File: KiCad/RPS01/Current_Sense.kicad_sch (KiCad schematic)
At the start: 4 parts, among them U8 INA139QPWRQ1

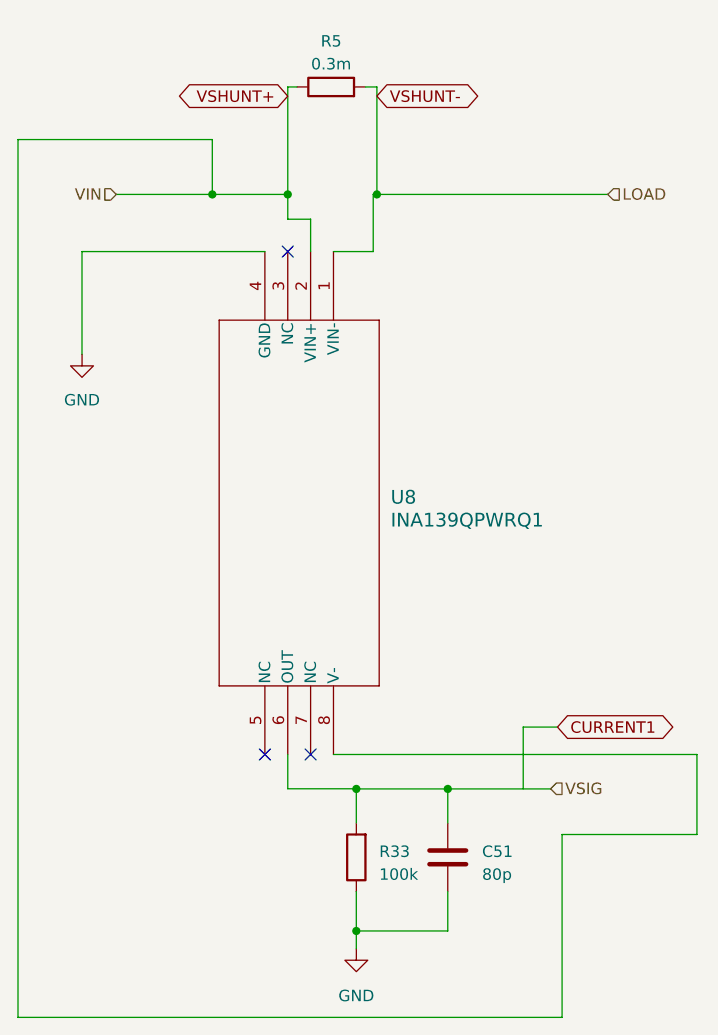
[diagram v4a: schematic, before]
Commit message: Finished Updating Footprints and Reorganized Reference Designators
Finished Updating Footprints and Reorganized Reference Designators

Starting to work on Final PCB, except for 19V Boost. Please check Schematic for errors
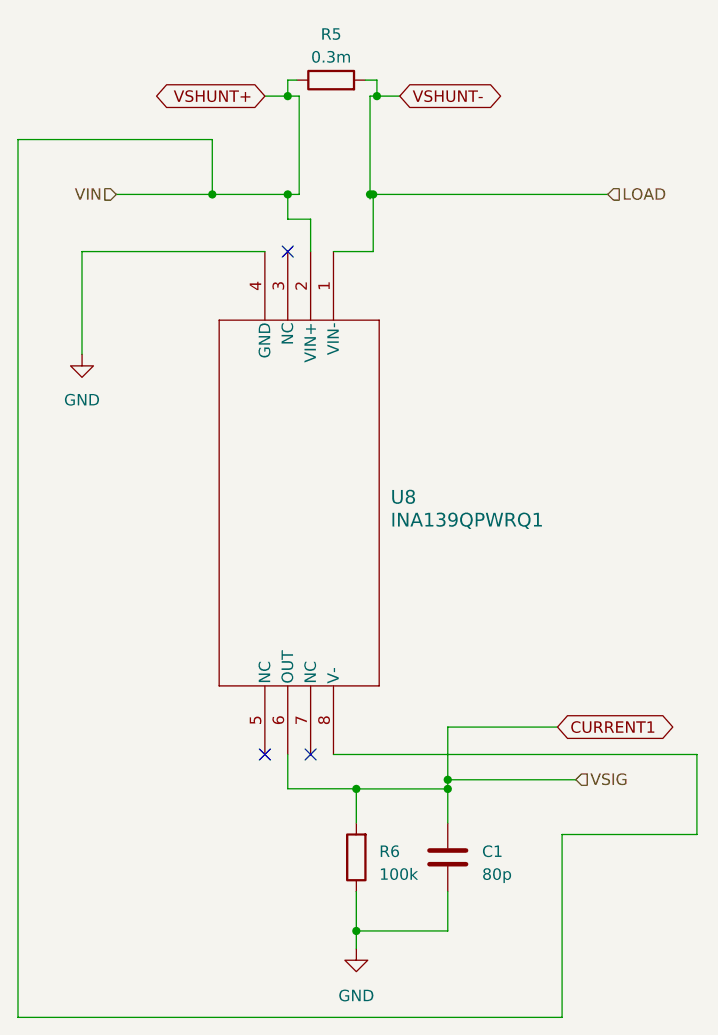
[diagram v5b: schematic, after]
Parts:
- renumbered C51 to C1, R33 to R6
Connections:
- net VSIG is gone; now on net CURRENT1: C1.1, R6.2, U8.6 (OUT)
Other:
- moved on the sheet: R5
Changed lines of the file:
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@@
 (kicad_sch (version 20230121) (generator eeschema)
   (paper "A4")
+  (junction (at 121.92 101.6158) (diameter 0) (color 0 0 0 0)
+  )
   (junction (at 104.14 35.56) (diameter 0) (color 0 0 0 0)
   )
   (junction (at 111.76 117.3986) (diameter 0) (color 0 0 0 0)
   )
+  (junction (at 114.046 24.638) (diameter 0) (color 0 0 0 0)
+  )
+  (junction (at 104.14 24.638) (diameter 0) (color 0 0 0 0)
+  )
   (junction (at 95.758 35.56) (diameter 0) (color 0 0 0 0)
   )
-  (junction (at 114.046 35.56) (diameter 0) (color 0 0 0 0)
+  (junction (at 113.284 35.56) (diameter 0) (color 0 0 0 0)
   )
-  (junction (at 121.92 101.6158) (diameter 0) (color 0 0 0 0)
+  (junction (at 113.6342 35.56) (diameter 0) (color 0 0 0 0)
   )
   (junction (at 111.76 101.6158) (diameter 0) (color 0 0 0 0)
   )
+  (junction (at 121.92 100.5998) (diameter 0) (color 0 0 0 0)
+  )
   (no_connect (at 101.6 97.79))
   (no_connect (at 104.14 41.91))
   (no_connect (at 106.68 97.79))
-  (wire (pts (xy 121.92 101.6158) (xy 133.35 101.6158))
+  (wire (pts (xy 105.41 24.638) (xy 104.14 24.638))
     (stroke (width 0) (type default))
   )
@@
     (stroke (width 0) (type default))
   )
-  (wire (pts (xy 105.156 23.622) (xy 104.14 23.622))
+  (wire (pts (xy 105.156 22.86) (xy 104.14 22.86))
     (stroke (width 0) (type default))
   )
-  (wire (pts (xy 114.046 23.622) (xy 114.046 35.56))
+  (wire (pts (xy 114.046 22.86) (xy 114.046 24.638))
     (stroke (width 0) (type default))
   )
@@
     (stroke (width 0) (type default))
   )
+  (wire (pts (xy 101.6 24.638) (xy 104.14 24.638))
+    (stroke (width 0) (type default))
+  )
+  (wire (pts (xy 121.92 101.6158) (xy 121.92 105.41))
+    (stroke (width 0) (type default))
+  )
   (wire (pts (xy 121.92 117.3986) (xy 111.76 117.3986))
     (stroke (width 0) (type default))
@@
     (stroke (width 0) (type default))
   )
-  (wire (pts (xy 104.14 23.622) (xy 104.14 35.56))
+  (wire (pts (xy 104.14 22.86) (xy 104.14 24.638))
     (stroke (width 0) (type default))
   )
@@
     (stroke (width 0) (type default))
   )
+  (wire (pts (xy 113.284 24.638) (xy 114.046 24.638))
+    (stroke (width 0) (type default))
+  )
   (wire (pts (xy 134.62 127) (xy 74.168 127))
     (stroke (width 0) (type default))
@@
     (stroke (width 0) (type default))
   )
-  (wire (pts (xy 112.776 23.622) (xy 114.046 23.622))
+  (wire (pts (xy 121.92 94.742) (xy 134.112 94.742))
+    (stroke (width 0) (type default))
+  )
+  (wire (pts (xy 113.284 35.56) (xy 113.6342 35.56))
+    (stroke (width 0) (type default))
+  )
+  (wire (pts (xy 112.776 22.86) (xy 114.046 22.86))
     (stroke (width 0) (type default))
   )
@@
     (stroke (width 0) (type default))
   )
-  (wire (pts (xy 113.6342 35.56) (xy 114.046 35.56))
+  (wire (pts (xy 116.586 24.638) (xy 114.046 24.638))
+    (stroke (width 0) (type default))
+  )
+  (wire (pts (xy 113.6342 35.56) (xy 139.7 35.56))
     (stroke (width 0) (type default))
   )
@@
     (stroke (width 0) (type default))
   )
+  (wire (pts (xy 121.92 94.742) (xy 121.92 100.5998))
+    (stroke (width 0) (type default))
+  )
   (wire (pts (xy 134.62 106.68) (xy 134.62 127))
     (stroke (width 0) (type default))
@@
     (stroke (width 0) (type default))
   )
-  (wire (pts (xy 133.35 101.6158) (xy 133.35 101.6))
+  (wire (pts (xy 136.144 100.5998) (xy 136.144 100.584))
     (stroke (width 0) (type default))
   )
@@
     (stroke (width 0) (type default))
   )
+  (wire (pts (xy 113.284 36.068) (xy 113.284 35.56))
+    (stroke (width 0) (type default))
+  )
+  (wire (pts (xy 105.41 35.56) (xy 104.14 35.56))
+    (stroke (width 0) (type default))
+  )
   (wire (pts (xy 81.28 41.91) (xy 81.28 53.34))
     (stroke (width 0) (type default))
   )
+  (wire (pts (xy 105.41 24.638) (xy 105.41 35.56))
+    (stroke (width 0) (type default))
+  )
   (wire (pts (xy 104.14 38.3106) (xy 104.14 35.56))
     (stroke (width 0) (type default))
@@
     (stroke (width 0) (type default))
   )
-  (wire (pts (xy 114.046 35.56) (xy 139.7 35.56))
-    (stroke (width 0) (type default))
-  )
-  (wire (pts (xy 130.302 101.6) (xy 130.302 94.742))
+  (wire (pts (xy 104.14 101.6) (xy 111.76 101.6))
     (stroke (width 0) (type default))
   )
-  (wire (pts (xy 104.14 101.6) (xy 111.76 101.6))
+  (wire (pts (xy 121.92 100.5998) (xy 121.92 101.6158))
     (stroke (width 0) (type default))
   )
-  (wire (pts (xy 130.302 94.742) (xy 134.112 94.742))
+  (wire (pts (xy 121.92 100.5998) (xy 136.144 100.5998))
     (stroke (width 0) (type default))
   )
-  (wire (pts (xy 121.92 101.6158) (xy 121.92 105.41))
+  (wire (pts (xy 113.284 24.638) (xy 113.284 35.56))
     (stroke (width 0) (type default))
   )
@@
     )
   )
-  (global_label "VSHUNT-" (shape bidirectional) (at 114.046 24.638 0) (fields_autoplaced)
+  (global_label "VSHUNT-" (shape bidirectional) (at 116.586 24.638 0) (fields_autoplaced)
     (effects (font (size 1.27 1.27)) (justify left))
-    (property "Intersheetrefs" "${INTERSHEET_REFS}" (at 126.8927 24.638 0)
+    (property "Intersheetrefs" "${INTERSHEET_REFS}" (at 129.4327 24.638 0)
       (effects (font (size 1.27 1.27)) (justify left) hide)
     )
   )
-  (global_label "VSHUNT+" (shape bidirectional) (at 104.14 24.638 180) (fields_autoplaced)
+  (global_label "VSHUNT+" (shape bidirectional) (at 101.6 24.638 180) (fields_autoplaced)
     (effects (font (size 1.27 1.27)) (justify right))
-    (property "Intersheetrefs" "${INTERSHEET_REFS}" (at 91.2933 24.638 0)
+    (property "Intersheetrefs" "${INTERSHEET_REFS}" (at 88.7533 24.638 0)
       (effects (font (size 1.27 1.27)) (justify right) hide)
     )
@@
     (effects (font (size 1.27 1.27)) (justify left))
   )
-  (hierarchical_label "VSIG" (shape input) (at 133.35 101.6 0) (fields_autoplaced)
+  (hierarchical_label "VSIG" (shape input) (at 136.144 100.584 0) (fields_autoplaced)
     (effects (font (size 1.27 1.27)) (justify left))
   )
@@
     )
   )
-  (symbol (lib_id "Device:R") (at 108.966 23.622 90) (unit 1)
+  (symbol (lib_id "Device:R") (at 108.966 22.86 90) (unit 1)
     (in_bom yes) (on_board yes) (dnp no) (fields_autoplaced)
-    (property "Reference" "R5" (at 108.966 18.542 90)
+    (property "Reference" "R5" (at 108.966 17.78 90)
       (effects (font (size 1.27 1.27)))
     )
-    (property "Value" "0.3m" (at 108.966 21.082 90)
+    (property "Value" "0.3m" (at 108.966 20.32 90)
       (effects (font (size 1.27 1.27)))
     )
-    (property "Footprint" "Mechatronic Footprints:CSS2H-5930R" (at 108.966 25.4 90)
+    (property "Footprint" "Mechatronic Footprints:CSS2H-5930R" (at 108.966 24.638 90)
       (effects (font (size 1.27 1.27)) hide)
     )
-    (property "Datasheet" "~" (at 108.966 23.622 0)
+    (property "Datasheet" "~" (at 108.966 22.86 0)
       (effects (font (size 1.27 1.27)) hide)
     )
@@
   (symbol (lib_id "Device:C") (at 121.92 109.22 0) (unit 1)
     (in_bom yes) (on_board yes) (dnp no) (fields_autoplaced)
-    (property "Reference" "C51" (at 125.73 108.585 0)
+    (property "Reference" "C1" (at 125.73 108.585 0)
       (effects (font (size 1.27 1.27)) (justify left))
     )
@@
       (project "rps01"
         (path "/14930f15-c0a0-4b55-93e6-b112548415f6/13e150ee-6c46-47a5-9c09-3749eb0dcbfe"
-          (reference "C51") (unit 1)
+          (reference "C1") (unit 1)
         )
       )
@@
   (symbol (lib_id "Device:R") (at 111.76 109.22 180) (unit 1)
     (in_bom yes) (on_board yes) (dnp no) (fields_autoplaced)
-    (property "Reference" "R33" (at 114.3 108.585 0)
+    (property "Reference" "R6" (at 114.3 108.585 0)
       (effects (font (size 1.27 1.27)) (justify right))
     )
@@
       (project "rps01"
         (path "/14930f15-c0a0-4b55-93e6-b112548415f6/13e150ee-6c46-47a5-9c09-3749eb0dcbfe"
-          (reference "R33") (unit 1)
+          (reference "R6") (unit 1)
         )
       )

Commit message: Board Ready For layout. Except for 19V Boost? CHECK vs SIM Please
Board Ready For layout. Except for 19V Boost? CHECK vs SIM Please
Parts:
- renumbered R6 to R5, R5 to R_S1
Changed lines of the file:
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@@
   (symbol (lib_id "power:GND") (at 81.28 53.34 0) (unit 1)
     (in_bom yes) (on_board yes) (dnp no) (fields_autoplaced)
-    (property "Reference" "#PWR012" (at 81.28 59.69 0)
+    (property "Reference" "#PWR014" (at 81.28 59.69 0)
       (effects (font (size 1.27 1.27)) hide)
     )
@@
       (project "rps01"
         (path "/14930f15-c0a0-4b55-93e6-b112548415f6/13e150ee-6c46-47a5-9c09-3749eb0dcbfe"
-          (reference "#PWR012") (unit 1)
+          (reference "#PWR014") (unit 1)
         )
       )
@@
   (symbol (lib_id "Device:R") (at 108.966 22.86 90) (unit 1)
     (in_bom yes) (on_board yes) (dnp no) (fields_autoplaced)
-    (property "Reference" "R5" (at 108.966 17.78 90)
+    (property "Reference" "R_S1" (at 108.966 17.78 90)
       (effects (font (size 1.27 1.27)))
     )
@@
       (project "rps01"
         (path "/14930f15-c0a0-4b55-93e6-b112548415f6/13e150ee-6c46-47a5-9c09-3749eb0dcbfe"
-          (reference "R5") (unit 1)
+          (reference "R_S1") (unit 1)
         )
       )
@@
   (symbol (lib_id "power:GND") (at 111.76 119.38 0) (unit 1)
     (in_bom yes) (on_board yes) (dnp no) (fields_autoplaced)
-    (property "Reference" "#PWR013" (at 111.76 125.73 0)
+    (property "Reference" "#PWR015" (at 111.76 125.73 0)
       (effects (font (size 1.27 1.27)) hide)
     )
@@
       (project "rps01"
         (path "/14930f15-c0a0-4b55-93e6-b112548415f6/13e150ee-6c46-47a5-9c09-3749eb0dcbfe"
-          (reference "#PWR013") (unit 1)
+          (reference "#PWR015") (unit 1)
         )
       )
@@
   (symbol (lib_id "Device:R") (at 111.76 109.22 180) (unit 1)
     (in_bom yes) (on_board yes) (dnp no) (fields_autoplaced)
-    (property "Reference" "R6" (at 114.3 108.585 0)
+    (property "Reference" "R5" (at 114.3 108.585 0)
       (effects (font (size 1.27 1.27)) (justify right))
     )
@@
       (project "rps01"
         (path "/14930f15-c0a0-4b55-93e6-b112548415f6/13e150ee-6c46-47a5-9c09-3749eb0dcbfe"
-          (reference "R6") (unit 1)
+          (reference "R5") (unit 1)
         )
       )

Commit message: Hotfix
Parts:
- added TP?: VSHUNT-, Mechatronics TestP:CONN1_RCU-0C_TEC, symbol Connector:TestPoint_Probe
- added TP?: VSHUNT+, Mechatronics TestP:CONN1_RCU-0C_TEC, symbol Connector:TestPoint_Probe
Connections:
- net VSHUNT+ renamed VIN
- net VIN: now also TP?.1
- net VSHUNT- renamed LOAD
- net LOAD: now also TP?.1
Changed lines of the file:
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@@
   (junction (at 111.76 117.3986) (diameter 0) (color 0 0 0 0)
   )
-  (junction (at 114.046 24.638) (diameter 0) (color 0 0 0 0)
+  (junction (at 114.554 35.56) (diameter 0) (color 0 0 0 0)
   )
   (junction (at 104.14 24.638) (diameter 0) (color 0 0 0 0)
@@
   (junction (at 95.758 35.56) (diameter 0) (color 0 0 0 0)
   )
-  (junction (at 113.284 35.56) (diameter 0) (color 0 0 0 0)
-  )
-  (junction (at 113.6342 35.56) (diameter 0) (color 0 0 0 0)
-  )
   (junction (at 111.76 101.6158) (diameter 0) (color 0 0 0 0)
   )
+  (junction (at 114.554 24.638) (diameter 0) (color 0 0 0 0)
+  )
   (junction (at 121.92 100.5998) (diameter 0) (color 0 0 0 0)
   )
@@
     (stroke (width 0) (type default))
   )
+  (wire (pts (xy 116.84 24.638) (xy 114.554 24.638))
+    (stroke (width 0) (type default))
+  )
   (wire (pts (xy 114.046 22.86) (xy 114.046 24.638))
     (stroke (width 0) (type default))
@@
     (stroke (width 0) (type default))
   )
-  (wire (pts (xy 101.6 24.638) (xy 104.14 24.638))
-    (stroke (width 0) (type default))
-  )
   (wire (pts (xy 121.92 101.6158) (xy 121.92 105.41))
     (stroke (width 0) (type default))
@@
     (stroke (width 0) (type default))
   )
+  (wire (pts (xy 95.758 24.638) (xy 104.14 24.638))
+    (stroke (width 0) (type default))
+  )
   (wire (pts (xy 111.76 117.3986) (xy 111.76 119.38))
     (stroke (width 0) (type default))
   )
+  (wire (pts (xy 114.554 24.638) (xy 114.046 24.638))
+    (stroke (width 0) (type default))
+  )
   (wire (pts (xy 104.14 22.86) (xy 104.14 24.638))
     (stroke (width 0) (type default))
@@
     (stroke (width 0) (type default))
   )
-  (wire (pts (xy 111.76 101.6158) (xy 121.92 101.6158))
+  (wire (pts (xy 114.554 35.56) (xy 114.554 41.91))
     (stroke (width 0) (type default))
   )
-  (wire (pts (xy 113.284 24.638) (xy 114.046 24.638))
+  (wire (pts (xy 111.76 101.6158) (xy 121.92 101.6158))
     (stroke (width 0) (type default))
   )
@@
     (stroke (width 0) (type default))
   )
-  (wire (pts (xy 113.284 35.56) (xy 113.6342 35.56))
-    (stroke (width 0) (type default))
-  )
   (wire (pts (xy 112.776 22.86) (xy 114.046 22.86))
     (stroke (width 0) (type default))
@@
     (stroke (width 0) (type default))
   )
-  (wire (pts (xy 116.586 24.638) (xy 114.046 24.638))
-    (stroke (width 0) (type default))
-  )
-  (wire (pts (xy 113.6342 35.56) (xy 139.7 35.56))
-    (stroke (width 0) (type default))
-  )
   (wire (pts (xy 95.758 29.464) (xy 95.758 35.56))
     (stroke (width 0) (type default))
@@
     (stroke (width 0) (type default))
   )
-  (wire (pts (xy 113.6342 41.91) (xy 109.22 41.91))
+  (wire (pts (xy 114.554 41.91) (xy 109.22 41.91))
     (stroke (width 0) (type default))
   )
@@
     (stroke (width 0) (type default))
   )
-  (wire (pts (xy 113.6342 35.56) (xy 113.6342 41.91))
+  (wire (pts (xy 114.554 24.638) (xy 114.554 35.56))
     (stroke (width 0) (type default))
   )
-  (wire (pts (xy 113.284 36.068) (xy 113.284 35.56))
+  (wire (pts (xy 114.554 35.56) (xy 139.7 35.56))
     (stroke (width 0) (type default))
   )
@@
     (stroke (width 0) (type default))
   )
-  (wire (pts (xy 121.92 100.5998) (xy 136.144 100.5998))
+  (wire (pts (xy 116.84 19.558) (xy 116.84 24.638))
     (stroke (width 0) (type default))
   )
-  (wire (pts (xy 113.284 24.638) (xy 113.284 35.56))
+  (wire (pts (xy 121.92 100.5998) (xy 136.144 100.5998))
     (stroke (width 0) (type default))
   )
@@
     )
   )
-  (global_label "VSHUNT-" (shape bidirectional) (at 116.586 24.638 0) (fields_autoplaced)
-    (effects (font (size 1.27 1.27)) (justify left))
-    (property "Intersheetrefs" "${INTERSHEET_REFS}" (at 129.4327 24.638 0)
-      (effects (font (size 1.27 1.27)) (justify left) hide)
-    )
-  )
-  (global_label "VSHUNT+" (shape bidirectional) (at 101.6 24.638 180) (fields_autoplaced)
-    (effects (font (size 1.27 1.27)) (justify right))
-    (property "Intersheetrefs" "${INTERSHEET_REFS}" (at 88.7533 24.638 0)
-      (effects (font (size 1.27 1.27)) (justify right) hide)
-    )
-  )
   (global_label "CURRENT1" (shape bidirectional) (at 134.112 94.742 0) (fields_autoplaced)
     (effects (font (size 1.27 1.27)) (justify left))
@@
     (effects (font (size 1.27 1.27)) (justify right))
   )
+  (symbol (lib_id "Connector:TestPoint_Probe") (at 116.84 19.558 0) (unit 1)
+    (in_bom yes) (on_board yes) (dnp no) (fields_autoplaced)
+    (property "Reference" "TP?" (at 121.158 17.3355 0)
+      (effects (font (size 1.27 1.27)) (justify left))
+    )
+    (property "Value" "VSHUNT-" (at 121.158 19.8755 0)
+      (effects (font (size 1.27 1.27)) (justify left))
+    )
+    (property "Footprint" "Mechatronics TestP:CONN1_RCU-0C_TEC" (at 121.92 19.558 0)
+      (effects (font (size 1.27 1.27)) hide)
+    )
+    (property "Datasheet" "~" (at 121.92 19.558 0)
+      (effects (font (size 1.27 1.27)) hide)
+    )
+    (pin "1")
+    (instances
+      (project "rps01"
+        (path "/14930f15-c0a0-4b55-93e6-b112548415f6/577d3fc4-735f-4981-a3a1-4300f23b9ae6"
+          (reference "TP?") (unit 1)
+        )
+        (path "/14930f15-c0a0-4b55-93e6-b112548415f6/13e150ee-6c46-47a5-9c09-3749eb0dcbfe"
+          (reference "TP1") (unit 1)
+        )
+      )
+    )
+  )
   (symbol (lib_id "power:GND") (at 81.28 53.34 0) (unit 1)
     (in_bom yes) (on_board yes) (dnp no) (fields_autoplaced)
@@
         )
       )
+    )
+  )
+  (symbol (lib_id "Connector:TestPoint_Probe") (at 95.758 24.638 0) (unit 1)
+    (in_bom yes) (on_board yes) (dnp no)
+    (property "Reference" "TP?" (at 93.726 17.272 0)
+      (effects (font (size 1.27 1.27)) (justify left))
+    )
+    (property "Value" "VSHUNT+" (at 92.456 19.304 0)
+      (effects (font (size 1.27 1.27)) (justify left))
+    )
+    (property "Footprint" "Mechatronics TestP:CONN1_RCU-0C_TEC" (at 100.838 24.638 0)
+      (effects (font (size 1.27 1.27)) hide)
+    )
+    (property "Datasheet" "~" (at 100.838 24.638 0)
+      (effects (font (size 1.27 1.27)) hide)
+    )
+    (pin "1")
+    (instances
+      (project "rps01"
+        (path "/14930f15-c0a0-4b55-93e6-b112548415f6/577d3fc4-735f-4981-a3a1-4300f23b9ae6"
+          (reference "TP?") (unit 1)
+        )
+        (path "/14930f15-c0a0-4b55-93e6-b112548415f6/13e150ee-6c46-47a5-9c09-3749eb0dcbfe"
+          (reference "TP2") (unit 1)
+        )
+      )
